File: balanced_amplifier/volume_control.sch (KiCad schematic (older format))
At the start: 57 parts, among them U5 LM4562, U6 LM4562, U7 LM4562, U8 LM4562

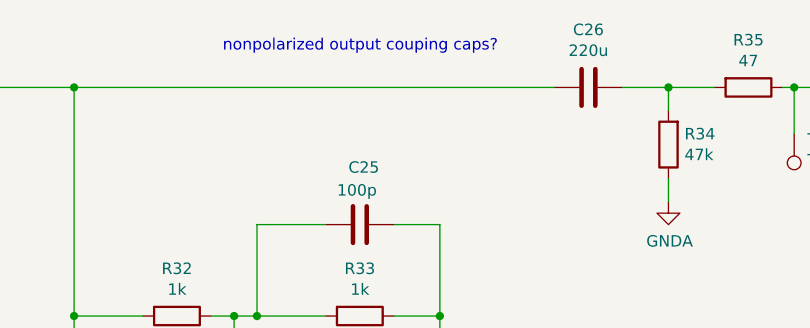
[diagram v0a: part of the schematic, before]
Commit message: Remove extraneous comment
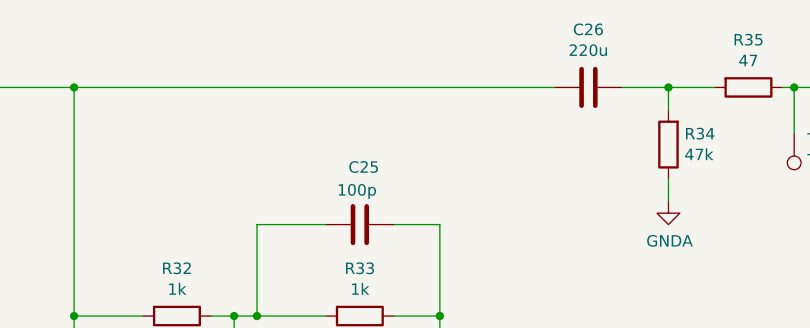
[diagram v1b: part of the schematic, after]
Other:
- note removed: "nonpolarized output couping caps?"
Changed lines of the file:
@@
 Wire Wire Line
 	5750 6500 5750 6900
-Text Notes 7100 750  0    50   ~ 0
-nonpolarized output couping caps?
 $Comp
 L Device:C C?

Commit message: Update footprint for C21, C28
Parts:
- C21, C28: footprint Capacitor_THT:CP_Radial_D5.0mm_P2.50mm -> Capacitor_THT:CP_Radial_D10.0mm_P5.00mm
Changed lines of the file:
@@
 F 0 "C21" V 1948 900 50  0000 C CNN
 F 1 "470u" V 2039 900 50  0000 C CNN
-F 2 "Capacitor_THT:CP_Radial_D5.0mm_P2.50mm" H 2200 900 50  0001 C CNN
+F 2 "Capacitor_THT:CP_Radial_D10.0mm_P5.00mm" H 2200 900 50  0001 C CNN
 F 3 "http://nichicon-us.com/english/products/pdfs/e-uvr.pdf" H 2200 900 50  0001 C CNN
 F 4 "Nichicon" H 2200 900 50  0001 C CNN "Manufacturer"
@@
 F 0 "C28" V 1948 4200 50  0000 C CNN
 F 1 "470u" V 2039 4200 50  0000 C CNN
-F 2 "Capacitor_THT:CP_Radial_D5.0mm_P2.50mm" H 2200 4200 50  0001 C CNN
+F 2 "Capacitor_THT:CP_Radial_D10.0mm_P5.00mm" H 2200 4200 50  0001 C CNN
 F 3 "http://nichicon-us.com/english/products/pdfs/e-uvr.pdf" H 2200 4200 50  0001 C CNN
 F 4 "Nichicon" H 2200 4200 50  0001 C CNN "Manufacturer"

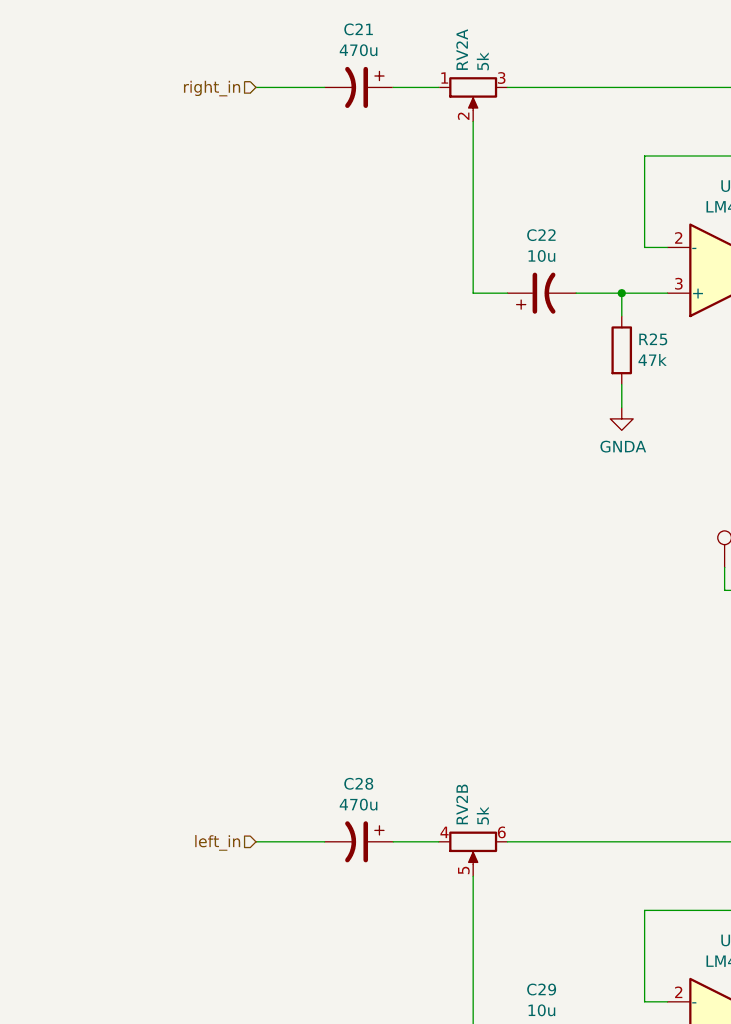
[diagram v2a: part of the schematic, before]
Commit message: Mirror volume control potentiometer so that turning volume CW increases volume
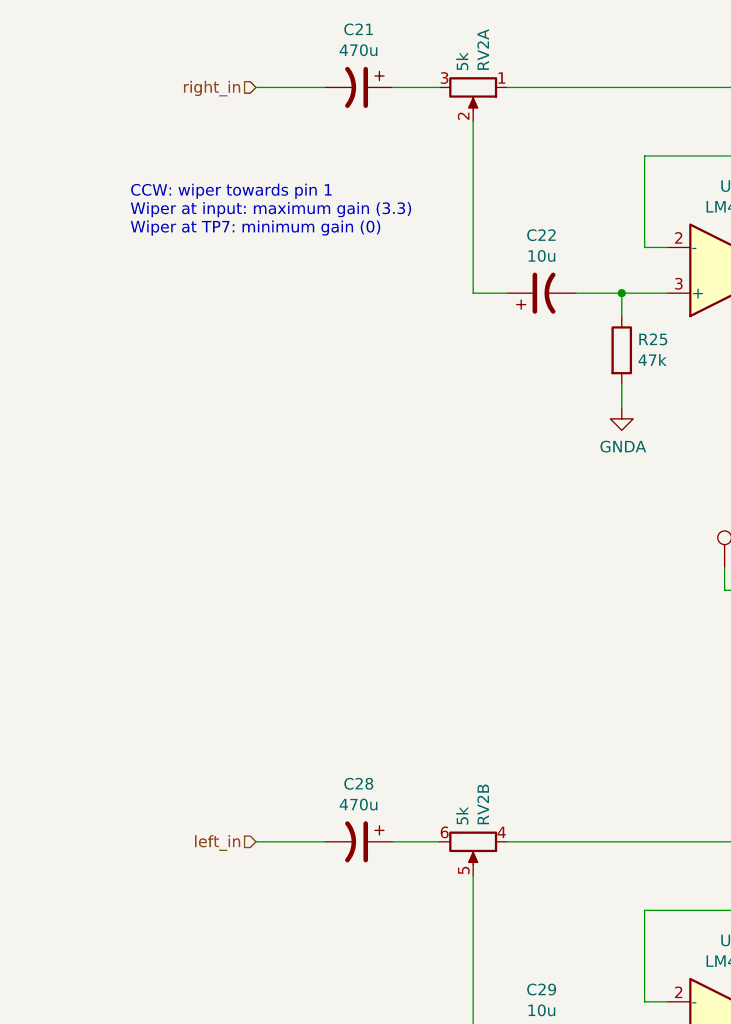
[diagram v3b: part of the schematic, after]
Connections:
- net at RV2.1: now also C26.2, R28.1, R31.1, R32.2, TP7.1; no longer C21.1
- net at RV2.4: now also C33.2, R41.1, R44.1, R45.2, TP11.1; no longer C28.1
- new net: C21.1, RV2.3
- new net: C28.1, RV2.6
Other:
- note added: "CCW: wiper towards pin 1\nWiper at input: maximum gain (3.3)\nWiper at TP7: minimum gain (0)"
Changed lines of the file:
@@
 F 9 "9.97" H 2700 900 50  0001 C CNN "Unit Price"
 	1    2700 900
-	0    -1   1    0
+	0    1    1    0
 $EndComp
 $Comp
@@
 F 9 "9.97" H 2700 4200 50  0001 C CNN "Unit Price"
 	2    2700 4200
-	0    -1   1    0
+	0    1    1    0
 $EndComp
 $Comp
@@
 Wire Wire Line
 	9600 5700 9750 5700
+Text Notes 1200 1550 0    50   ~ 0
+CCW: wiper towards pin 1\nWiper at input: maximum gain (3.3)\nWiper at TP7: minimum gain (0)
 $EndSCHEMATC

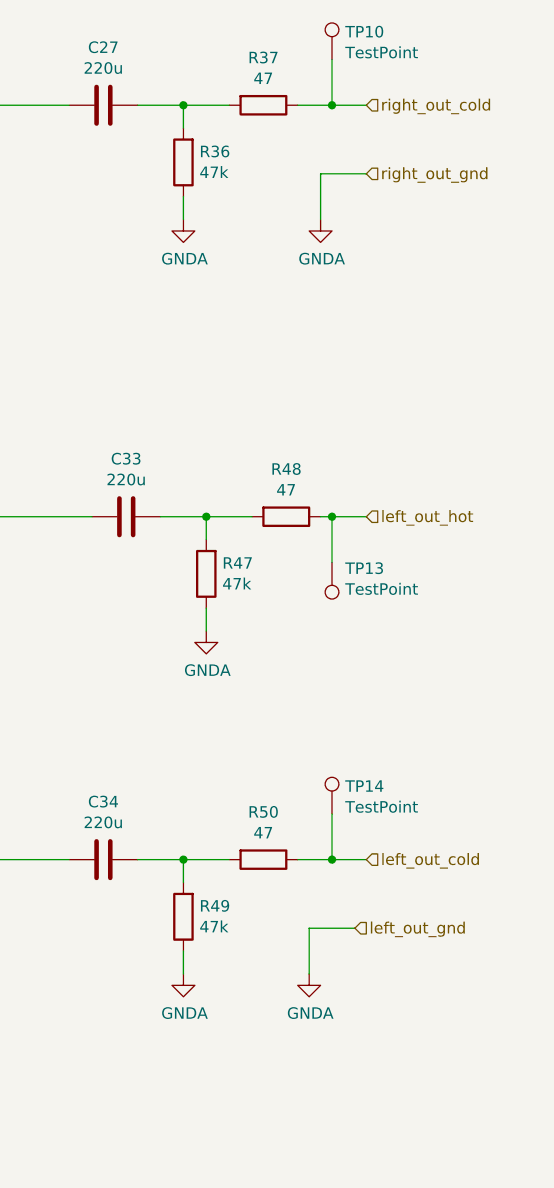
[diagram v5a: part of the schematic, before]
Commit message: update balanced amplifier input/output/power connectors
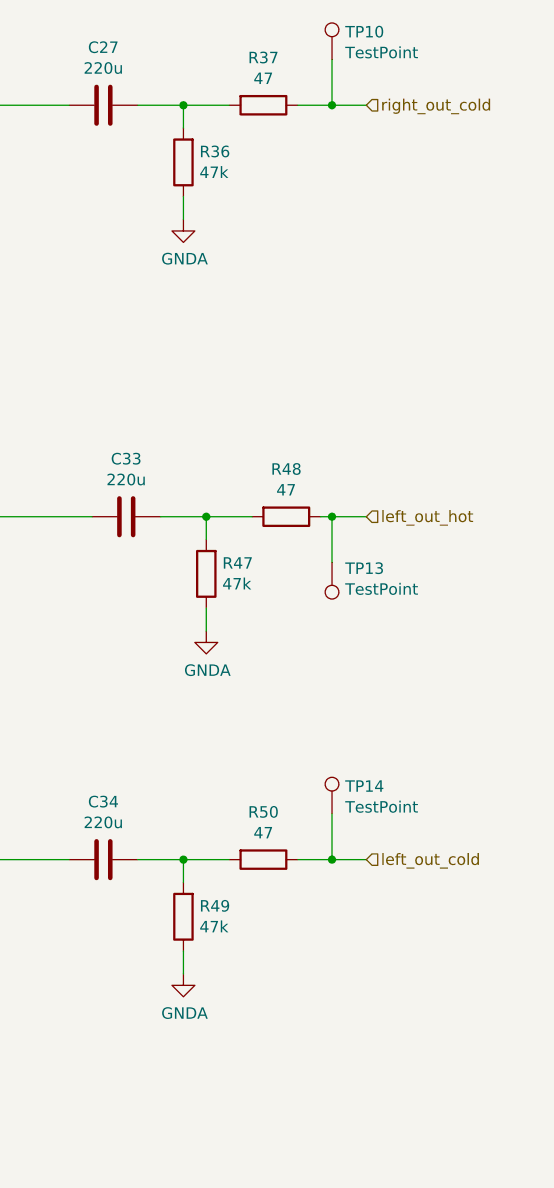
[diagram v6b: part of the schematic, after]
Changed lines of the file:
@@
 Text HLabel 1750 4200 0    50   Input ~ 0
 left_in
-Text HLabel 9750 2700 2    50   Input ~ 0
-right_out_gnd
-Text HLabel 9700 6000 2    50   Input ~ 0
-left_out_gnd
 Wire Wire Line
 	9450 2400 9600 2400
-$Comp
-L power:GNDA #PWR?
-U 1 1 5C073E57
-P 9550 2900
-AR Path="/5BE4EEC1/5C073E57" Ref="#PWR?"  Part="1"
-AR Path="/5BF8808C/5C073E57" Ref="#PWR0126"  Part="1"
-F 0 "#PWR0126" H 9550 2650 50  0001 C CNN
-F 1 "GNDA" H 9555 2727 50  0000 C CNN
-F 2 "" H 9550 2900 50  0001 C CNN
-F 3 "" H 9550 2900 50  0001 C CNN
-	1    9550 2900
-	1    0    0    -1
-$EndComp
-Wire Wire Line
-	9550 2900 9550 2700
-Wire Wire Line
-	9550 2700 9750 2700
 Wire Wire Line
 	2700 4350 2700 5100
@@
 $Comp
 L power:GNDA #PWR?
-U 1 1 5C1CDB68
-P 9500 6200
-AR Path="/5BE4EEC1/5C1CDB68" Ref="#PWR?"  Part="1"
-AR Path="/5BF8808C/5C1CDB68" Ref="#PWR0132"  Part="1"
-F 0 "#PWR0132" H 9500 5950 50  0001 C CNN
-F 1 "GNDA" H 9505 6027 50  0000 C CNN
-F 2 "" H 9500 6200 50  0001 C CNN
-F 3 "" H 9500 6200 50  0001 C CNN
-	1    9500 6200
-	1    0    0    -1
-$EndComp
-Wire Wire Line
-	9500 6200 9500 6000
-Wire Wire Line
-	9500 6000 9700 6000
-$Comp
-L power:GNDA #PWR?

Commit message: update footprint for volume/balance pots
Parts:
- RV2: footprint Potentiometer_THT_custom:Potentiometer_Bourns_91_Dual_Horizontal -> Potentiometer_THT_custom:Potentiometer_Bourns_91A2x-x28-xxx_Dual_Horizontal
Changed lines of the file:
@@
 F 0 "RV2" H 2630 946 50  0000 R CNN
 F 1 "5k" H 2630 855 50  0000 R CNN
-F 2 "Potentiometer_THT_custom:Potentiometer_Bourns_91_Dual_Horizontal" H 2700 900 50  0001 C CNN
+F 2 "Potentiometer_THT_custom:Potentiometer_Bourns_91A2x-x28-xxx_Dual_Horizontal" H 2700 900 50  0001 C CNN
 F 3 "https://www.bourns.com/docs/Product-Datasheets/91_95.pdf" H 2700 900 50  0001 C CNN
 F 4 "Bourns" H 2700 900 50  0001 C CNN "Manufacturer"
@@
 F 0 "RV2" H 2630 4246 50  0000 R CNN
 F 1 "5k" H 2630 4155 50  0000 R CNN
-F 2 "Potentiometer_THT_custom:Potentiometer_Bourns_91_Dual_Horizontal" H 2700 4200 50  0001 C CNN
+F 2 "Potentiometer_THT_custom:Potentiometer_Bourns_91A2x-x28-xxx_Dual_Horizontal" H 2700 4200 50  0001 C CNN
 F 3 "https://www.bourns.com/docs/Product-Datasheets/91_95.pdf" H 2700 4200 50  0001 C CNN
 F 4 "Bourns" H 2700 4200 50  0001 C CNN "Manufacturer"
